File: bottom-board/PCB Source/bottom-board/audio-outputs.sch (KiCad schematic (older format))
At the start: 53 parts, among them P11 JACK_TRS_6PINS, P12 JACK_TRS_6PINS, U6 OPA1678, U7 OPA1678

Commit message: update fabrication data
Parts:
- C41, C45: footprint Capacitor_SMD:C_0603_1608Metric -> Capacitor_SMD:C_0805_2012Metric; MPN EMK107BBJ106MA-T -> GRM219R61E106KA12D
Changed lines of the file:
@@
 F 0 "C41" H 2505 7100 50  0000 R CNN
 F 1 "10uF" H 2335 7010 50  0000 L CNN
-F 2 "Capacitor_SMD:C_0603_1608Metric" H 2605 7080 60  0001 C CNN
+F 2 "Capacitor_SMD:C_0805_2012Metric" H 2605 7080 60  0001 C CNN
 F 3 "" H 2605 7080 60  0000 C CNN
-F 4 "EMK107BBJ106MA-T" H -1845 5380 50  0001 C CNN "MPN"
+F 4 "GRM219R61E106KA12D" H -1845 5380 50  0001 C CNN "MPN"
 	1    2605 7080
 	-1   0    0    1
@@
 F 0 "C45" H 3425 7090 50  0000 R CNN
 F 1 "10uF" H 3255 7000 50  0000 L CNN
-F 2 "Capacitor_SMD:C_0603_1608Metric" H 3525 7070 60  0001 C CNN
+F 2 "Capacitor_SMD:C_0805_2012Metric" H 3525 7070 60  0001 C CNN
 F 3 "" H 3525 7070 60  0000 C CNN
-F 4 "EMK107BBJ106MA-T" H -925 5370 50  0001 C CNN "MPN"
+F 4 "GRM219R61E106KA12D" H -925 5370 50  0001 C CNN "MPN"
 	1    3525 7070
 	-1   0    0    1

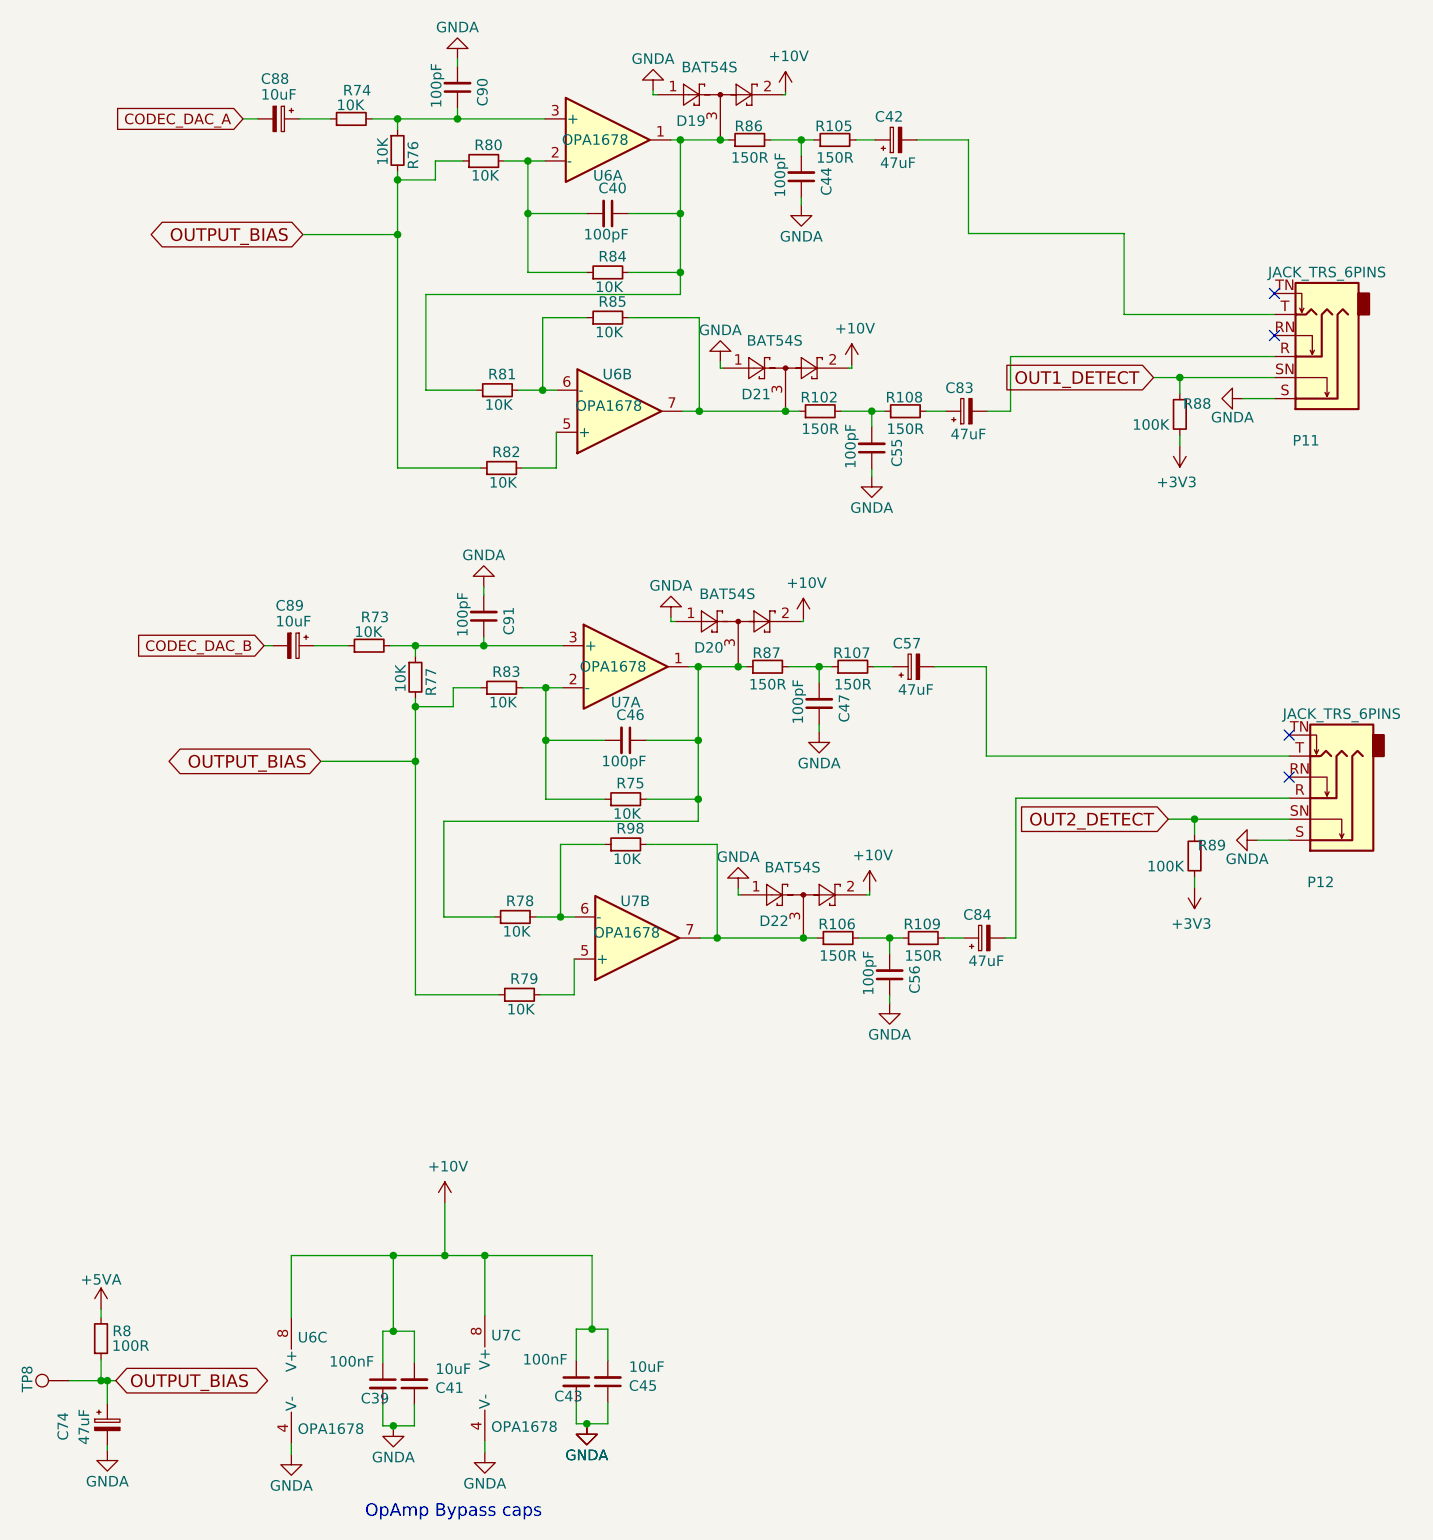
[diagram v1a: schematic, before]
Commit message: change input bias 5->6V, reduce harmonics
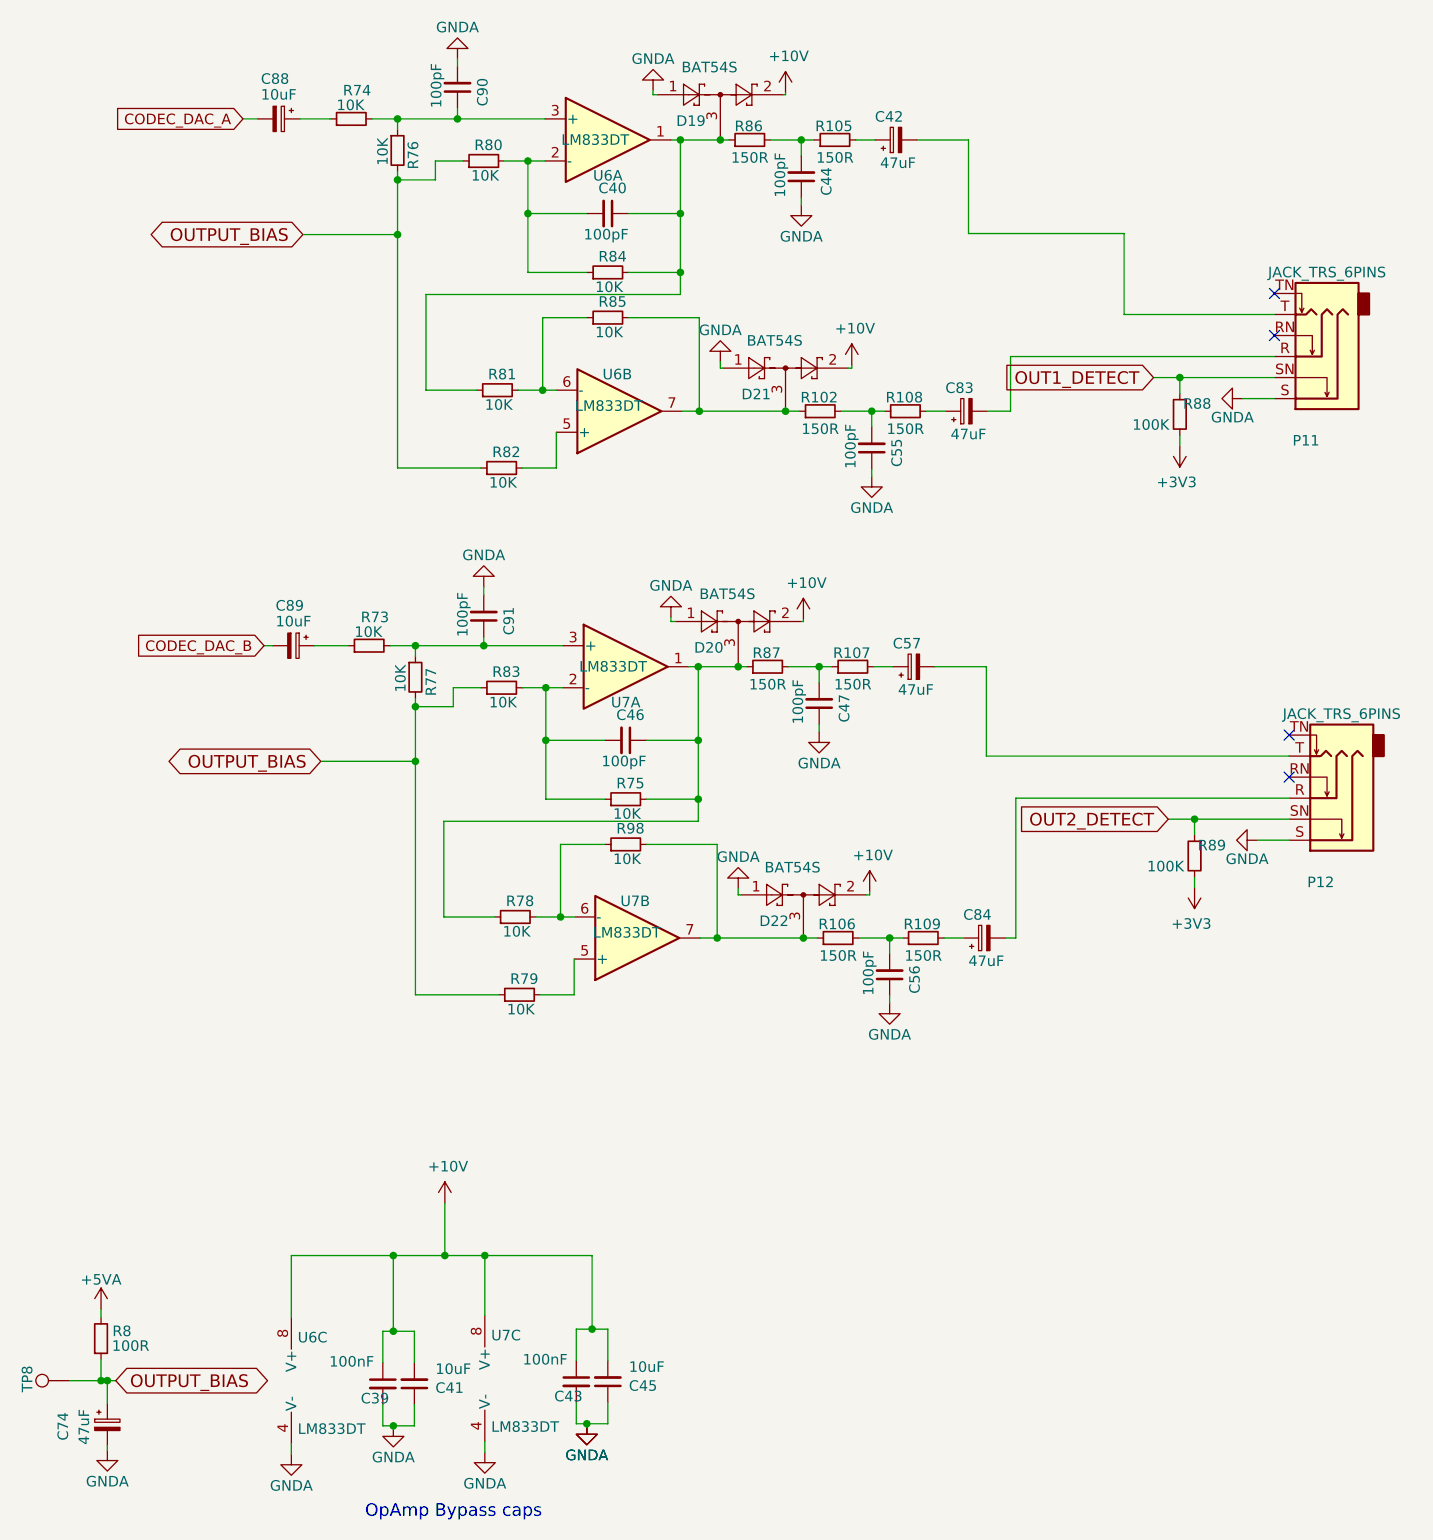
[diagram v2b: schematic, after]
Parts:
- U6, U7: value OPA1678 -> LM833DT
- U6: value OPA1678 -> LM833DT; MPN TL082CDR -> LM833DT
- U7: value OPA1678 -> LM833DT; MPN OPA1678IDR -> LM833DT
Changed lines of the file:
@@
 AR Path="/54F72CD0/5F3E612A" Ref="U6"  Part="1"
 F 0 "U6" H 3525 995 50  0000 C CNN
-F 1 "OPA1678" H 3465 1165 50  0000 C CNN
+F 1 "LM833DT" H 3465 1165 50  0000 C CNN
 F 2 "Package_SO:SOIC-8_3.9x4.9mm_P1.27mm" H 3525 1165 50  0001 C CNN
 F 3 "http://www.ti.com/lit/ds/symlink/tl071.pdf" H 3525 1165 50  0001 C CNN
@@
 AR Path="/54F72CD0/5F40E337" Ref="U6"  Part="3"
 F 0 "U6" H 2050 7270 50  0000 L CNN
-F 1 "OPA1678" H 2050 6835 50  0000 L CNN
+F 1 "LM833DT" H 2050 6835 50  0000 L CNN
 F 2 "Package_SO:SOIC-8_3.9x4.9mm_P1.27mm" H 2120 7065 50  0001 C CNN
 F 3 "http://www.ti.com/lit/ds/symlink/tl071.pdf" H 2120 7065 50  0001 C CNN
@@
 AR Path="/54F72CD0/5F416511" Ref="U7"  Part="3"
 F 0 "U7" H 2970 7260 50  0000 L CNN
-F 1 "OPA1678" H 2970 6825 50  0000 L CNN
+F 1 "LM833DT" H 2970 6825 50  0000 L CNN
 F 2 "Package_SO:SOIC-8_3.9x4.9mm_P1.27mm" H 3040 7055 50  0001 C CNN
 F 3 "http://www.ti.com/lit/ds/symlink/tl071.pdf" H 3040 7055 50  0001 C CNN
@@
 AR Path="/54F72CD0/5F42AAEA" Ref="U6"  Part="2"
 F 0 "U6" H 3570 2280 50  0000 C CNN
-F 1 "OPA1678" H 3530 2430 50  0000 C CNN
+F 1 "LM833DT" H 3530 2430 50  0000 C CNN
 F 2 "Package_SO:SOIC-8_3.9x4.9mm_P1.27mm" H 3580 2455 50  0001 C CNN
 F 3 "http://www.ti.com/lit/ds/symlink/tl071.pdf" H 3580 2455 50  0001 C CNN
-F 4 "TL082CDR" H 3580 2455 50  0001 C CNN "MPN"
+F 4 "LM833DT" H 3580 2455 50  0001 C CNN "MPN"
 	2    3580 2455
 	1    0    0    1
@@
 AR Path="/54F72CD0/5F4F37D9" Ref="U7"  Part="2"
 F 0 "U7" H 3655 4785 50  0000 C CNN
-F 1 "OPA1678" H 3615 4935 50  0000 C CNN
+F 1 "LM833DT" H 3615 4935 50  0000 C CNN
 F 2 "Package_SO:SOIC-8_3.9x4.9mm_P1.27mm" H 3665 4960 50  0001 C CNN
 F 3 "http://www.ti.com/lit/ds/symlink/tl071.pdf" H 3665 4960 50  0001 C CNN
@@
 AR Path="/54F72CD0/5F4F37B6" Ref="U7"  Part="1"
 F 0 "U7" H 3610 3500 50  0000 C CNN
-F 1 "OPA1678" H 3550 3670 50  0000 C CNN
+F 1 "LM833DT" H 3550 3670 50  0000 C CNN
 F 2 "Package_SO:SOIC-8_3.9x4.9mm_P1.27mm" H 3610 3670 50  0001 C CNN
 F 3 "http://www.ti.com/lit/ds/symlink/tl071.pdf" H 3610 3670 50  0001 C CNN
-F 4 "OPA1678IDR" H 3610 3670 50  0001 C CNN "MPN"
+F 4 "LM833DT" H 3610 3670 50  0001 C CNN "MPN"
 	1    3610 3670
 	1    0    0    -1

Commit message: correct MPN R112, U6 and U7
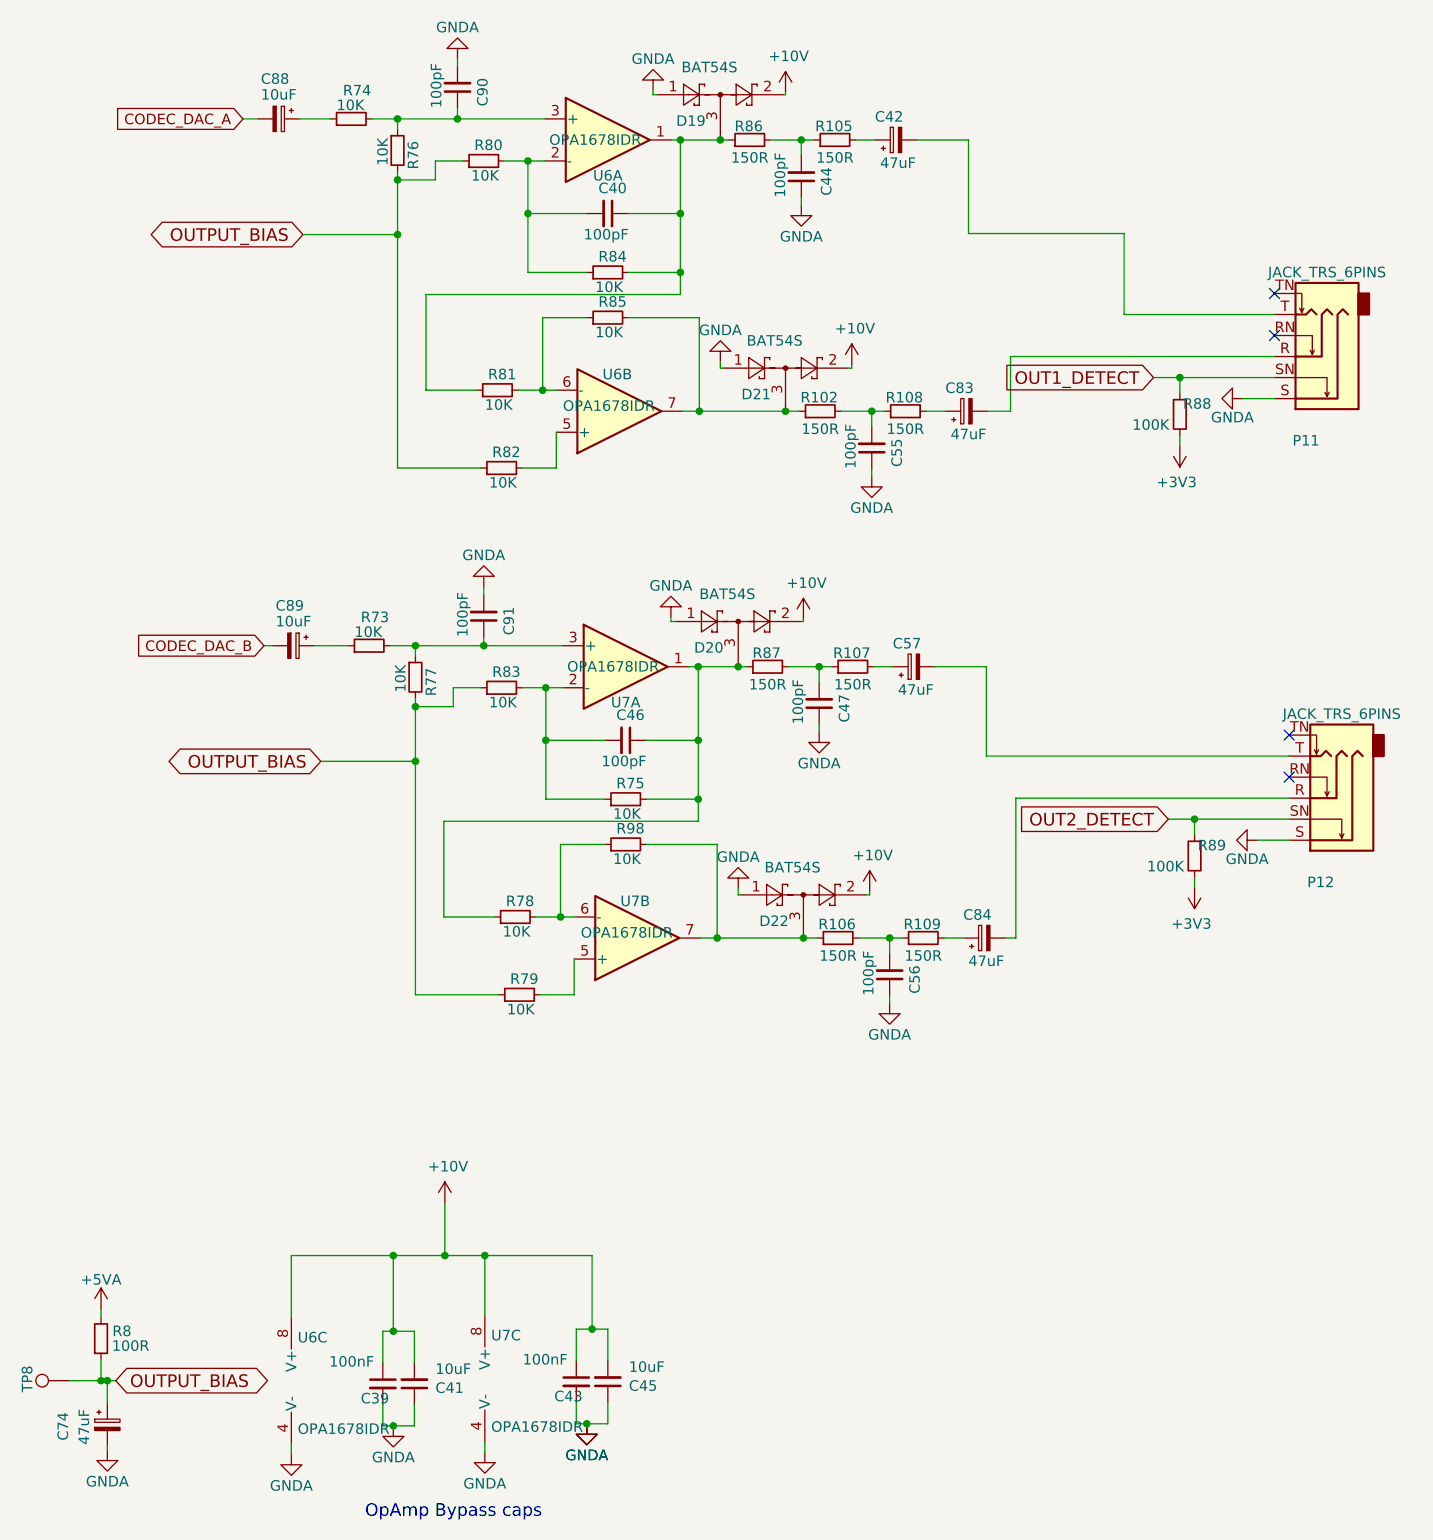
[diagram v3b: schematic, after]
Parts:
- U6, U7: value LM833DT -> OPA1678IDR
- U7: value LM833DT -> OPA1678IDR; MPN (none) -> OPA1678IDR
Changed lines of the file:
@@
 AR Path="/54F72CD0/5F3E612A" Ref="U6"  Part="1"
 F 0 "U6" H 3525 995 50  0000 C CNN
-F 1 "LM833DT" H 3465 1165 50  0000 C CNN
+F 1 "OPA1678IDR" H 3465 1165 50  0000 C CNN
 F 2 "Package_SO:SOIC-8_3.9x4.9mm_P1.27mm" H 3525 1165 50  0001 C CNN
 F 3 "http://www.ti.com/lit/ds/symlink/tl071.pdf" H 3525 1165 50  0001 C CNN
@@
 AR Path="/54F72CD0/5F40E337" Ref="U6"  Part="3"
 F 0 "U6" H 2050 7270 50  0000 L CNN
-F 1 "LM833DT" H 2050 6835 50  0000 L CNN
+F 1 "OPA1678IDR" H 2050 6835 50  0000 L CNN
 F 2 "Package_SO:SOIC-8_3.9x4.9mm_P1.27mm" H 2120 7065 50  0001 C CNN
 F 3 "http://www.ti.com/lit/ds/symlink/tl071.pdf" H 2120 7065 50  0001 C CNN
@@
 AR Path="/54F72CD0/5F416511" Ref="U7"  Part="3"
 F 0 "U7" H 2970 7260 50  0000 L CNN
-F 1 "LM833DT" H 2970 6825 50  0000 L CNN
+F 1 "OPA1678IDR" H 2970 6825 50  0000 L CNN
 F 2 "Package_SO:SOIC-8_3.9x4.9mm_P1.27mm" H 3040 7055 50  0001 C CNN
 F 3 "http://www.ti.com/lit/ds/symlink/tl071.pdf" H 3040 7055 50  0001 C CNN
+F 4 "OPA1678IDR" H 3040 7055 50  0001 C CNN "MPN"
 	3    3040 7055
 	1    0    0    -1
@@
 AR Path="/54F72CD0/5F42AAEA" Ref="U6"  Part="2"
 F 0 "U6" H 3570 2280 50  0000 C CNN
-F 1 "LM833DT" H 3530 2430 50  0000 C CNN
+F 1 "OPA1678IDR" H 3530 2430 50  0000 C CNN
 F 2 "Package_SO:SOIC-8_3.9x4.9mm_P1.27mm" H 3580 2455 50  0001 C CNN
 F 3 "http://www.ti.com/lit/ds/symlink/tl071.pdf" H 3580 2455 50  0001 C CNN
@@
 AR Path="/54F72CD0/5F4F37D9" Ref="U7"  Part="2"
 F 0 "U7" H 3655 4785 50  0000 C CNN
-F 1 "LM833DT" H 3615 4935 50  0000 C CNN
+F 1 "OPA1678IDR" H 3615 4935 50  0000 C CNN
 F 2 "Package_SO:SOIC-8_3.9x4.9mm_P1.27mm" H 3665 4960 50  0001 C CNN
 F 3 "http://www.ti.com/lit/ds/symlink/tl071.pdf" H 3665 4960 50  0001 C CNN
@@
 AR Path="/54F72CD0/5F4F37B6" Ref="U7"  Part="1"
 F 0 "U7" H 3610 3500 50  0000 C CNN
-F 1 "LM833DT" H 3550 3670 50  0000 C CNN
+F 1 "OPA1678IDR" H 3550 3670 50  0000 C CNN
 F 2 "Package_SO:SOIC-8_3.9x4.9mm_P1.27mm" H 3610 3670 50  0001 C CNN
 F 3 "http://www.ti.com/lit/ds/symlink/tl071.pdf" H 3610 3670 50  0001 C CNN
